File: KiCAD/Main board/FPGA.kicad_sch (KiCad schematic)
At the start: 0 parts

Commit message: Worked on KiCAD
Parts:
- added J10: GPIO 0, Connector_PinHeader_2.54mm:PinHeader_2x20_P2.54mm_Vertical, symbol Connector_Generic:Conn_02x20_Odd_Even
- added J11: GPIO 1, Connector_PinHeader_2.54mm:PinHeader_2x20_P2.54mm_Vertical, symbol Connector_Generic:Conn_02x20_Odd_Even
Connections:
- new net GND: J10.12 (Pin_12), J10.30 (Pin_30), J11.12 (Pin_12), J11.30 (Pin_30)
- no-connect marks 0 -> 4
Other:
- note added: "Update to schrouded headers like on the FPGA board"
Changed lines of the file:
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@@
 (kicad_sch (version 20230121) (generator eeschema)
   (paper "A4")
+  (junction (at 120.65 77.47) (diameter 0) (color 0 0 0 0)
+  )
+  (junction (at 66.04 76.2) (diameter 0) (color 0 0 0 0)
+  )
+  (no_connect (at 50.8 76.2))
+  (no_connect (at 50.8 53.34))
+  (no_connect (at 105.41 54.61))
+  (no_connect (at 105.41 77.47))
+  (wire (pts (xy 118.11 54.61) (xy 120.65 54.61))
+    (stroke (width 0) (type default))
+  )
+  (wire (pts (xy 66.04 90.17) (xy 66.04 76.2))
+    (stroke (width 0) (type default))
+  )
+  (wire (pts (xy 120.65 54.61) (xy 120.65 77.47))
+    (stroke (width 0) (type default))
+  )
+  (wire (pts (xy 66.04 53.34) (xy 66.04 76.2))
+    (stroke (width 0) (type default))
+  )
+  (wire (pts (xy 63.5 53.34) (xy 66.04 53.34))
+    (stroke (width 0) (type default))
+  )
+  (wire (pts (xy 120.65 91.44) (xy 120.65 77.47))
+    (stroke (width 0) (type default))
+  )
+  (wire (pts (xy 63.5 76.2) (xy 66.04 76.2))
+    (stroke (width 0) (type default))
+  )
+  (wire (pts (xy 118.11 77.47) (xy 120.65 77.47))
+    (stroke (width 0) (type default))
+  )
+  (text "Update to schrouded headers like on the FPGA board"
+    (at 54.61 31.75 0)
+    (effects (font (size 1.27 1.27)) (justify left bottom))
+  )
+  (symbol (lib_id "power:GND") (at 66.04 90.17 0) (unit 1)
+    (in_bom yes) (on_board yes) (dnp no) (fields_autoplaced)
+    (property "Reference" "#PWR0101" (at 66.04 96.52 0)
+      (effects (font (size 1.27 1.27)) hide)
+    )
+    (property "Value" "GND" (at 66.04 95.25 0)
+      (effects (font (size 1.27 1.27)))
+    )
+    (property "Footprint" "" (at 66.04 90.17 0)
+      (effects (font (size 1.27 1.27)) hide)
+    )
+    (property "Datasheet" "" (at 66.04 90.17 0)
+      (effects (font (size 1.27 1.27)) hide)
+    )
+    (pin "1")
+    (instances
+      (project "Main board"
+        (path "/2f8cbac6-fd11-4240-8e40-3bb6952a0324/22c0a18e-6cf4-4154-962a-243bb7c27459"
+          (reference "#PWR0101") (unit 1)
+        )
+      )
+    )
+  )
+  (symbol (lib_id "Connector_Generic:Conn_02x20_Odd_Even") (at 55.88 63.5 0) (unit 1)
+    (in_bom yes) (on_board yes) (dnp no) (fields_autoplaced)
+    (property "Reference" "J10" (at 57.15 35.56 0)
+      (effects (font (size 1.27 1.27)))
+    )
+    (property "Value" "GPIO 0" (at 57.15 38.1 0)
+      (effects (font (size 1.27 1.27)))
+    )
+    (property "Footprint" "Connector_PinHeader_2.54mm:PinHeader_2x20_P2.54mm_Vertical" (at 55.88 63.5 0)
+      (effects (font (size 1.27 1.27)) hide)
+    )
+    (property "Datasheet" "~" (at 55.88 63.5 0)
+      (effects (font (size 1.27 1.27)) hide)
+    )
+    (pin "1")
+    (pin "10")
+    (pin "11")
+    (pin "12")
+    (pin "13")
+    (pin "14")
+    (pin "15")
+    (pin "16")
+    (pin "17")
+    (pin "18")
+    (pin "19")
+    (pin "2")
+    (pin "20")
+    (pin "21")
+    (pin "22")
+    (pin "23")
+    (pin "24")
+    (pin "25")
+    (pin "26")
+    (pin "27")
+    (pin "28")
+    (pin "29")
+    (pin "3")
+    (pin "30")
+    (pin "31")
+    (pin "32")
+    (pin "33")
+    (pin "34")
+    (pin "35")
+    (pin "36")
+    (pin "37")
+    (pin "38")
+    (pin "39")
+    (pin "4")
+    (pin "40")
+    (pin "5")
+    (pin "6")
+    (pin "7")
+    (pin "8")
+    (pin "9")
+    (instances
+      (project "Main board"
+        (path "/2f8cbac6-fd11-4240-8e40-3bb6952a0324/22c0a18e-6cf4-4154-962a-243bb7c27459"
+          (reference "J10") (unit 1)
+        )
+      )
+    )
+  )
+  (symbol (lib_id "Connector_Generic:Conn_02x20_Odd_Even") (at 110.49 64.77 0) (unit 1)
+    (in_bom yes) (on_board yes) (dnp no) (fields_autoplaced)
+    (property "Reference" "J11" (at 111.76 36.83 0)
+      (effects (font (size 1.27 1.27)))
+    )
+    (property "Value" "GPIO 1" (at 111.76 39.37 0)
+      (effects (font (size 1.27 1.27)))
+    )
+    (property "Footprint" "Connector_PinHeader_2.54mm:PinHeader_2x20_P2.54mm_Vertical" (at 110.49 64.77 0)
+      (effects (font (size 1.27 1.27)) hide)
+    )
+    (property "Datasheet" "~" (at 110.49 64.77 0)
+      (effects (font (size 1.27 1.27)) hide)
+    )
+    (pin "1")
+    (pin "10")
+    (pin "11")
+    (pin "12")
+    (pin "13")
+    (pin "14")
+    (pin "15")
+    (pin "16")
+    (pin "17")
+    (pin "18")
+    (pin "19")
+    (pin "2")
+    (pin "20")
+    (pin "21")
+    (pin "22")
+    (pin "23")
+    (pin "24")
+    (pin "25")
+    (pin "26")
+    (pin "27")
+    (pin "28")
+    (pin "29")
+    (pin "3")
+    (pin "30")
+    (pin "31")
+    (pin "32")
+    (pin "33")
+    (pin "34")
+    (pin "35")
+    (pin "36")
+    (pin "37")
+    (pin "38")
+    (pin "39")
+    (pin "4")
+    (pin "40")
+    (pin "5")
+    (pin "6")
+    (pin "7")
+    (pin "8")
+    (pin "9")
+    (instances
+      (project "Main board"
+        (path "/2f8cbac6-fd11-4240-8e40-3bb6952a0324/22c0a18e-6cf4-4154-962a-243bb7c27459"
+          (reference "J11") (unit 1)
+        )
+      )
+    )
+  )
+  (symbol (lib_id "power:GND") (at 120.65 91.44 0) (unit 1)
+    (in_bom yes) (on_board yes) (dnp no) (fields_autoplaced)
+    (property "Reference" "#PWR0102" (at 120.65 97.79 0)
+      (effects (font (size 1.27 1.27)) hide)
+    )
+    (property "Value" "GND" (at 120.65 96.52 0)
+      (effects (font (size 1.27 1.27)))
+    )
+    (property "Footprint" "" (at 120.65 91.44 0)
+      (effects (font (size 1.27 1.27)) hide)
+    )
+    (property "Datasheet" "" (at 120.65 91.44 0)
+      (effects (font (size 1.27 1.27)) hide)
+    )
+    (pin "1")
+    (instances
+      (project "Main board"
+        (path "/2f8cbac6-fd11-4240-8e40-3bb6952a0324/22c0a18e-6cf4-4154-962a-243bb7c27459"
+          (reference "#PWR0102") (unit 1)
+        )
+      )
+    )
+  )
 )

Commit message: Worked a bit on the main board
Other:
- note added: "DAC"
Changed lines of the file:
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@@
     (stroke (width 0) (type default))
+  )
+  (text "DAC" (at 190.5 59.69 0)
+    (effects (font (size 1.27 1.27) bold) (justify left bottom))
   )
   (text "Update to schrouded headers like on the FPGA board"
@@
     (effects (font (size 1.27 1.27)) (justify left bottom))
   )
+  (hierarchical_label "RST_CH1_2" (shape output) (at 168.91 59.69 0) (fields_autoplaced)
+    (effects (font (size 1.27 1.27)) (justify left))
+  )
+  (hierarchical_label "DIN_CH1_2" (shape output) (at 168.91 54.61 0) (fields_autoplaced)
+    (effects (font (size 1.27 1.27)) (justify left))
+  )
+  (hierarchical_label "SCL_CH1_2" (shape output) (at 168.91 67.31 0) (fields_autoplaced)
+    (effects (font (size 1.27 1.27)) (justify left))
+  )
+  (hierarchical_label "BCK_CH1_2" (shape output) (at 168.91 52.07 0) (fields_autoplaced)
+    (effects (font (size 1.27 1.27)) (justify left))
+  )
+  (hierarchical_label "SDA_CH1_2" (shape bidirectional) (at 168.91 64.77 0) (fields_autoplaced)
+    (effects (font (size 1.27 1.27)) (justify left))
+  )
+  (hierarchical_label "AMUTEI_CH1_2" (shape output) (at 168.91 62.23 0) (fields_autoplaced)
+    (effects (font (size 1.27 1.27)) (justify left))
+  )
+  (hierarchical_label "LRCK_CH1_2" (shape output) (at 168.91 49.53 0) (fields_autoplaced)
+    (effects (font (size 1.27 1.27)) (justify left))
+  )
+  (hierarchical_label "SCKI_CH1_2" (shape output) (at 168.91 57.15 0) (fields_autoplaced)
+    (effects (font (size 1.27 1.27)) (justify left))
+  )
   (symbol (lib_id "power:GND") (at 66.04 90.17 0) (unit 1)

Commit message: Worked on main board
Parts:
- J10, J11: footprint Connector_PinHeader_2.54mm:PinHeader_2x20_P2.54mm_Vertical -> Connector_IDC:IDC-Header_2x20_P2.54mm_Vertical
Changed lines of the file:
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@@
       (effects (font (size 1.27 1.27)))
     )
-    (property "Footprint" "Connector_PinHeader_2.54mm:PinHeader_2x20_P2.54mm_Vertical" (at 55.88 63.5 0)
+    (property "Footprint" "Connector_IDC:IDC-Header_2x20_P2.54mm_Vertical" (at 55.88 63.5 0)
       (effects (font (size 1.27 1.27)) hide)
     )
@@
       (effects (font (size 1.27 1.27)))
     )
-    (property "Footprint" "Connector_PinHeader_2.54mm:PinHeader_2x20_P2.54mm_Vertical" (at 110.49 64.77 0)
+    (property "Footprint" "Connector_IDC:IDC-Header_2x20_P2.54mm_Vertical" (at 110.49 64.77 0)
       (effects (font (size 1.27 1.27)) hide)
     )

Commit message: Worked on main board
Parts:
- renumbered J10 to J13, J11 to J14
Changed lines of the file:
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@@
   (symbol (lib_id "power:GND") (at 66.04 90.17 0) (unit 1)
     (in_bom yes) (on_board yes) (dnp no) (fields_autoplaced)
-    (property "Reference" "#PWR0101" (at 66.04 96.52 0)
+    (property "Reference" "#PWR0171" (at 66.04 96.52 0)
       (effects (font (size 1.27 1.27)) hide)
     )
@@
       (project "Main board"
         (path "/2f8cbac6-fd11-4240-8e40-3bb6952a0324/22c0a18e-6cf4-4154-962a-243bb7c27459"
-          (reference "#PWR0101") (unit 1)
+          (reference "#PWR0171") (unit 1)
         )
       )
@@
   (symbol (lib_id "Connector_Generic:Conn_02x20_Odd_Even") (at 55.88 63.5 0) (unit 1)
     (in_bom yes) (on_board yes) (dnp no) (fields_autoplaced)
-    (property "Reference" "J10" (at 57.15 35.56 0)
+    (property "Reference" "J13" (at 57.15 38.1 0)
       (effects (font (size 1.27 1.27)))
     )
@@
       (project "Main board"
         (path "/2f8cbac6-fd11-4240-8e40-3bb6952a0324/22c0a18e-6cf4-4154-962a-243bb7c27459"
-          (reference "J10") (unit 1)
+          (reference "J13") (unit 1)
         )
       )
@@
   (symbol (lib_id "Connector_Generic:Conn_02x20_Odd_Even") (at 110.49 64.77 0) (unit 1)
     (in_bom yes) (on_board yes) (dnp no) (fields_autoplaced)
-    (property "Reference" "J11" (at 111.76 36.83 0)
+    (property "Reference" "J14" (at 111.76 39.37 0)
       (effects (font (size 1.27 1.27)))
     )
@@
       (project "Main board"
         (path "/2f8cbac6-fd11-4240-8e40-3bb6952a0324/22c0a18e-6cf4-4154-962a-243bb7c27459"
-          (reference "J11") (unit 1)
+          (reference "J14") (unit 1)
         )
       )
@@
   (symbol (lib_id "power:GND") (at 120.65 91.44 0) (unit 1)
     (in_bom yes) (on_board yes) (dnp no) (fields_autoplaced)
-    (property "Reference" "#PWR0102" (at 120.65 97.79 0)
+    (property "Reference" "#PWR0170" (at 120.65 97.79 0)
       (effects (font (size 1.27 1.27)) hide)
     )
@@
       (project "Main board"
         (path "/2f8cbac6-fd11-4240-8e40-3bb6952a0324/22c0a18e-6cf4-4154-962a-243bb7c27459"
-          (reference "#PWR0102") (unit 1)
+          (reference "#PWR0170") (unit 1)
         )
       )

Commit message: fixed symbols excluding from board
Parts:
- J13, J14: footprint Connector_IDC:IDC-Header_2x20_P2.54mm_Vertical -> (none)
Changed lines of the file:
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@@
       (effects (font (size 1.27 1.27)))
     )
-    (property "Footprint" "Connector_IDC:IDC-Header_2x20_P2.54mm_Vertical" (at 55.88 63.5 0)
+    (property "Footprint" "" (at 55.88 63.5 0)
       (effects (font (size 1.27 1.27)) hide)
     )
@@
       (effects (font (size 1.27 1.27)))
     )
-    (property "Footprint" "Connector_IDC:IDC-Header_2x20_P2.54mm_Vertical" (at 110.49 64.77 0)
+    (property "Footprint" "" (at 110.49 64.77 0)
       (effects (font (size 1.27 1.27)) hide)
     )

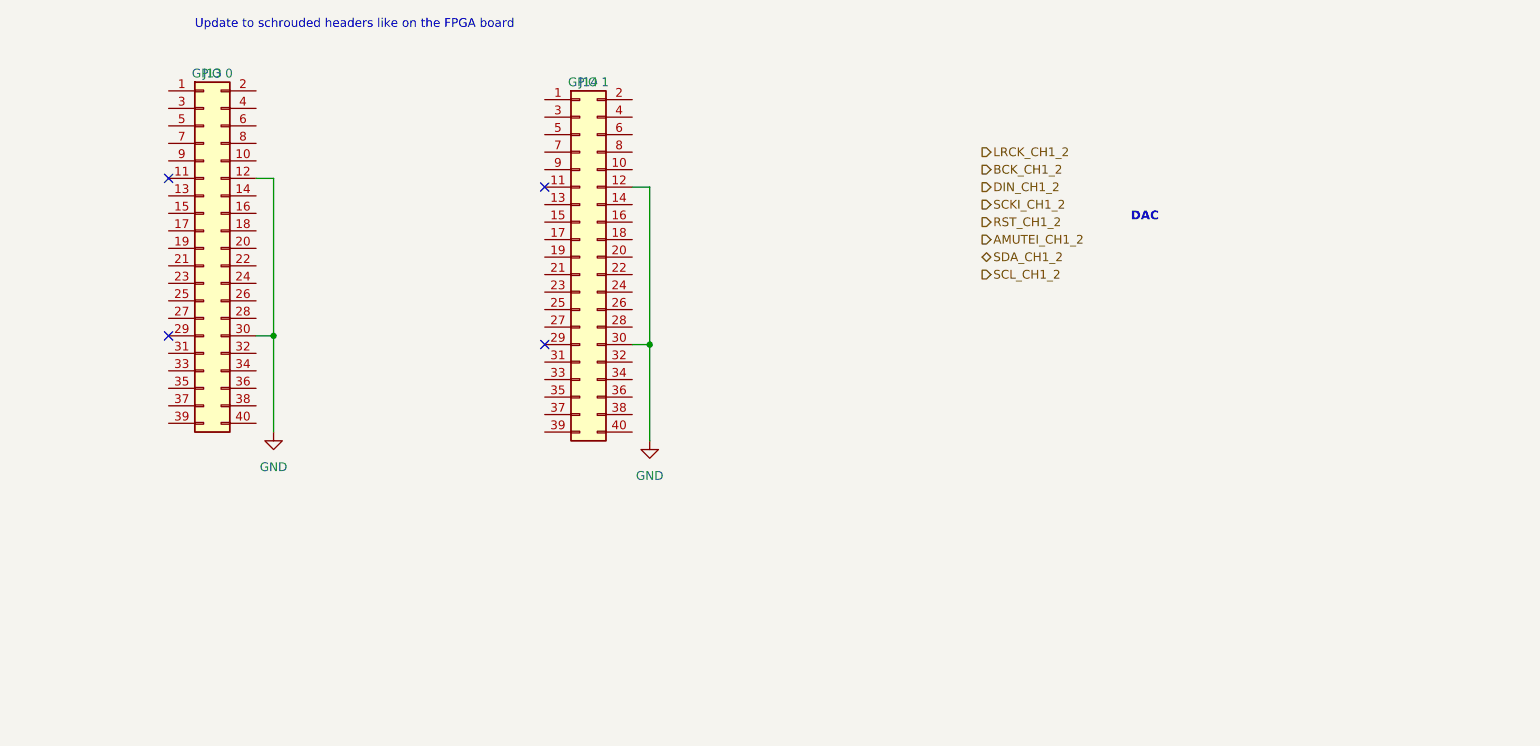
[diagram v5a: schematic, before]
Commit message: Made symbol and footprint for the FPGA board
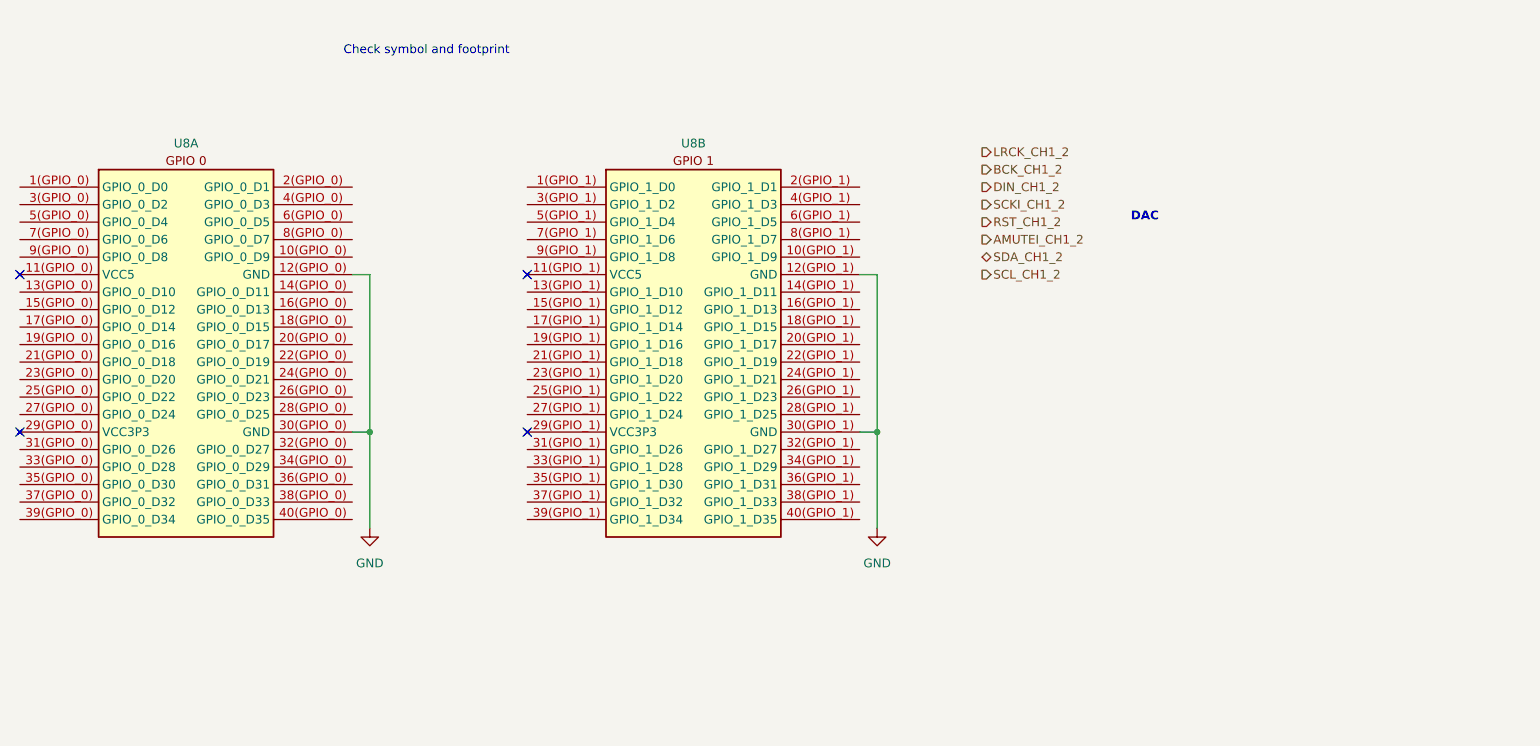
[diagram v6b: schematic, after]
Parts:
- removed J13: GPIO 0, symbol Connector_Generic:Conn_02x20_Odd_Even
- removed J14: GPIO 1, symbol Connector_Generic:Conn_02x20_Odd_Even
- added U8: ~, Audio-DSP:DE1-SoC, symbol Audio_DSP:DE1-SoC
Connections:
- net GND: now also U8.12(GPIO_0) (GND), U8.12(GPIO_1) (GND), U8.30(GPIO_0) (GND), U8.30(GPIO_1) (GND)
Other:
- note added: "Check symbol and footprint"
- note removed: "Update to schrouded headers like on the FPGA board"

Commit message: Worked on main board SCH
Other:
- note added: "Check symbol and footprint with someone else"
- note removed: "Check symbol and footprint"
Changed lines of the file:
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@@
     (effects (font (size 1.27 1.27) bold) (justify left bottom))
   )
-  (text "Check symbol and footprint" (at 76.2 35.56 0)
+  (text "Check symbol and footprint with someone else" (at 76.2 35.56 0)
     (effects (font (size 1.27 1.27) (color 255 0 0 1)) (justify left bottom))
   )
